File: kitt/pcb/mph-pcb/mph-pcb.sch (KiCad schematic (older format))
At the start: 121 parts, among them J1 Screw_Terminal_01x02, J2 Screw_Terminal_01x03, U1 TLC5940NT, U2 TLC5940NT, U3 TLC5940NT, U4 TLC5940NT, U5 TLC5940NT, U6 TLC5940NT, U7 TLC5940NT

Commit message: sed to get flangeless led
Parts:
- D25, D26, D27, HT1, HT10, HT11, HT12, HT13, HT14, HT15, HT16, HT2, HT3, HT4, HT5, HT6, HT7, HT8, HT9, HY1, HY2, HY3, MY1, MY2, MY3, UG1, UG10, UG11, UG12, UG13, UG14, UG15, UG16, UG17, UG18, UG19, UG2, UG20, UG3, UG4, UG5, UG6, UG7, UG8, UG9, UGY1, UGY2, UGY3: footprint (none) -> KITT-Footpads:Flangeless_LED

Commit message: added screw terminals
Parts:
- GUID1, GUID2, SYST1, SYST2: footprint (none) -> KITT-Footpads:DF3GD_Light_Bar
- J1: footprint (none) -> KITT-Footpads:5mm_Screw_Terminal_01x02
- J2: footprint (none) -> KITT-Footpads:5mm_Screw_Terminal_01x03
- MPH1, MPH2, MPH3: footprint (none) -> KITT-Footpads:KB2855SGD_Light_Square
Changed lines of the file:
@@
 F 0 "SYST2" H 9628 5046 50  0000 L CNN
 F 1 "DF3GD" H 9628 4955 50  0000 L CNN
-F 2 "" H 9500 5350 50  0001 C CNN
+F 2 "KITT-Footpads:DF3GD_Light_Bar" H 9500 5350 50  0001 C CNN
 F 3 "" H 9500 5350 50  0001 C CNN
 	1    9300 5000
@@
 F 0 "SYST1" H 8578 5046 50  0000 L CNN
 F 1 "DF3GD" H 8578 4955 50  0000 L CNN
-F 2 "" H 8450 5350 50  0001 C CNN
+F 2 "KITT-Footpads:DF3GD_Light_Bar" H 8450 5350 50  0001 C CNN
 F 3 "" H 8450 5350 50  0001 C CNN
 	1    8250 5000
@@
 F 0 "GUID2" H 9628 3696 50  0000 L CNN
 F 1 "DF3GD" H 9628 3605 50  0000 L CNN
-F 2 "" H 9500 4000 50  0001 C CNN
+F 2 "KITT-Footpads:DF3GD_Light_Bar" H 9500 4000 50  0001 C CNN
 F 3 "" H 9500 4000 50  0001 C CNN
 	1    9300 3650
@@
 F 0 "GUID1" H 8578 3696 50  0000 L CNN
 F 1 "DF3GD" H 8578 3605 50  0000 L CNN
-F 2 "" H 8450 4000 50  0001 C CNN
+F 2 "KITT-Footpads:DF3GD_Light_Bar" H 8450 4000 50  0001 C CNN
 F 3 "" H 8450 4000 50  0001 C CNN
 	1    8250 3650
@@
 F 0 "J1" H 1618 13467 50  0000 C CNN
 F 1 "Screw_Terminal_01x02" H 1618 13376 50  0000 C CNN
-F 2 "" H 1700 13250 50  0001 C CNN
+F 2 "KITT-Footpads:5mm_Screw_Terminal_01x02" H 1700 13250 50  0001 C CNN
 F 3 "~" H 1700 13250 50  0001 C CNN
 	1    1700 13250
@@
 F 0 "MPH1" H 18228 4546 50  0000 L CNN
 F 1 "KB2855SGD" H 18228 4455 50  0000 L CNN
-F 2 "" H 17400 4600 50  0001 C CNN
+F 2 "KITT-Footpads:KB2855SGD_Light_Square" H 17400 4600 50  0001 C CNN
 F 3 "" H 17400 4600 50  0001 C CNN
 	1    17800 4500
@@
 F 0 "MPH2" H 19528 4546 50  0000 L CNN
 F 1 "KB2855SGD" H 19528 4455 50  0000 L CNN
-F 2 "" H 18700 4600 50  0001 C CNN
+F 2 "KITT-Footpads:KB2855SGD_Light_Square" H 18700 4600 50  0001 C CNN
 F 3 "" H 18700 4600 50  0001 C CNN
 	1    19100 4500
@@
 F 0 "MPH3" H 20828 4546 50  0000 L CNN
 F 1 "KB2855SGD" H 20828 4455 50  0000 L CNN
-F 2 "" H 20000 4600 50  0001 C CNN
+F 2 "KITT-Footpads:KB2855SGD_Light_Square" H 20000 4600 50  0001 C CNN
 F 3 "" H 20000 4600 50  0001 C CNN
 	1    20400 4500
@@
 F 0 "J2" H 1668 14817 50  0000 C CNN
 F 1 "Screw_Terminal_01x03" H 1668 14726 50  0000 C CNN
-F 2 "" H 1750 14500 50  0001 C CNN
+F 2 "KITT-Footpads:5mm_Screw_Terminal_01x03" H 1750 14500 50  0001 C CNN
 F 3 "~" H 1750 14500 50  0001 C CNN
 	1    1750 14500

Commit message: add footpad for logic level shifter
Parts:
- LVL1: footprint (none) -> KITT-Footpads:LVL_5V_3V3
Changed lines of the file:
@@
 F 0 "LVL1" H 3250 15025 50  0000 C CNN
 F 1 "LVL_5V_3V3" H 3250 14934 50  0000 C CNN
-F 2 "" H 3250 14500 50  0001 C CNN
+F 2 "KITT-Footpads:LVL_5V_3V3" H 3250 14500 50  0001 C CNN
 F 3 "" H 3250 14500 50  0001 C CNN
 	1    3250 14500

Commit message: initial placement
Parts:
- renumbered D25 to MSGY1, D26 to MSGY2, D27 to MSGY3
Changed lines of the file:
@@
 	11750 1850 11750 1450
 $Comp
-L Device:LED D25
+L Device:LED MSGY1
 U 1 1 619E187B
 P 11750 6050
-F 0 "D25" V 11789 5932 50  0000 R CNN
+F 0 "MSGY1" V 11789 5932 50  0000 R CNN
 F 1 "LED" V 11698 5932 50  0000 R CNN
 F 2 "KITT-Footpads:Flangeless_LED" H 11750 6050 50  0001 C CNN
@@
 $EndComp
 $Comp
-L Device:LED D26
+L Device:LED MSGY2
 U 1 1 619E1881
 P 12100 6050
-F 0 "D26" V 12139 5932 50  0000 R CNN
+F 0 "MSGY2" V 12139 5932 50  0000 R CNN
 F 1 "LED" V 12048 5932 50  0000 R CNN
 F 2 "KITT-Footpads:Flangeless_LED" H 12100 6050 50  0001 C CNN
@@
 $EndComp
 $Comp
-L Device:LED D27
+L Device:LED MSGY3
 U 1 1 619E1887
 P 12450 6050
-F 0 "D27" V 12489 5932 50  0000 R CNN
+F 0 "MSGY3" V 12489 5932 50  0000 R CNN
 F 1 "LED" V 12398 5932 50  0000 R CNN
 F 2 "KITT-Footpads:Flangeless_LED" H 12450 6050 50  0001 C CNN

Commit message: add net ties for coupling caps
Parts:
- added NT1, NT2, NT3, NT4, NT5, NT6, NT7: Net-Tie_3_Tee, NetTie:NetTie-3_THT_Pad0.3mm, symbol Device:Net-Tie_3_Tee
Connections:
- net +5V: now also NT1.1, NT2.1, NT3.1, NT4.1, NT5.1, NT6.1, NT7.1; no longer C3.1, C4.1, C5.1, C6.1, C7.1, C8.1, C9.1, U1.21 (VCC), U2.21 (VCC), U3.21 (VCC), U4.21 (VCC), U5.21 (VCC), U6.21 (VCC), U7.21 (VCC)
- new net: NT1.2, U1.21 (VCC)
- new net: C3.1, NT1.3
- new net: NT2.2, U2.21 (VCC)
- new net: NT3.2, U3.21 (VCC)
- new net: C4.1, NT2.3
- new net: C5.1, NT3.3
- new net: C6.1, NT4.3
- new net: NT4.2, U4.21 (VCC)
- new net: NT5.2, U5.21 (VCC)
- new net: NT6.2, U6.21 (VCC)
- new net: C7.1, NT5.3
- new net: NT7.2, U7.21 (VCC)
- new net: C8.1, NT6.3
- new net: C9.1, NT7.3
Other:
- moved on the sheet: C3, C4, C5, C6, C7, C8, C9

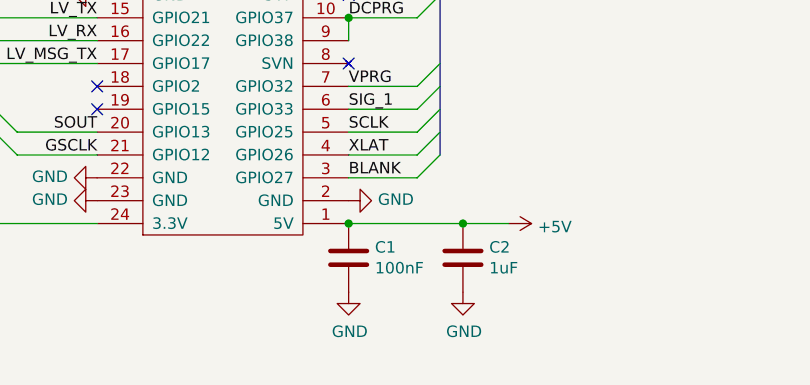
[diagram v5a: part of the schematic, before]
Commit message: routed led display chips
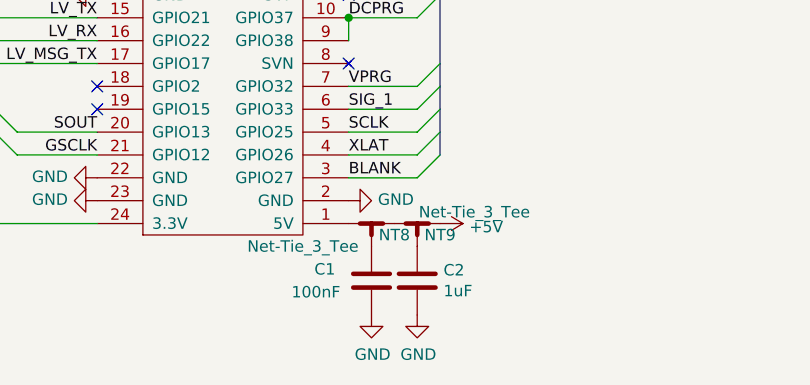
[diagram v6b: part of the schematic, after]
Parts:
- added NT8, NT9: Net-Tie_3_Tee, symbol Device:Net-Tie_3_Tee
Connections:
- net +5V: now also NT9.2; no longer C1.1, C2.1, TTGO1.1 (5V)
- new net: NT8.1, TTGO1.1 (5V)
- new net: C2.1, NT9.3
- new net: C1.1, NT8.3
- new net: NT8.2, NT9.1
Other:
- moved on the sheet: C1, C2
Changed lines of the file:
@@
 L power:+5V #PWR0108
 U 1 1 61112410
-P 6450 15300
-F 0 "#PWR0108" H 6450 15150 50  0001 C CNN
-F 1 "+5V" V 6465 15428 50  0000 L CNN
-F 2 "" H 6450 15300 50  0001 C CNN
-F 3 "" H 6450 15300 50  0001 C CNN
-	1    6450 15300
+P 6150 15300
+F 0 "#PWR0108" H 6150 15150 50  0001 C CNN
+F 1 "+5V" V 6165 15428 50  0000 L CNN
+F 2 "" H 6150 15300 50  0001 C CNN
+F 3 "" H 6150 15300 50  0001 C CNN
+	1    6150 15300
 	0    1    1    0
 $EndComp
@@
 	1    0    0    -1
 $EndComp
-Wire Wire Line
-	5750 15300 6250 15300
 $Comp
 L Device:C C1
 U 1 1 611E1B9E
-P 5750 15450
-F 0 "C1" H 5865 15496 50  0000 L CNN
-F 1 "100nF" H 5865 15405 50  0000 L CNN
-F 2 "Capacitor_THT:C_Rect_L7.0mm_W3.5mm_P5.00mm" H 5788 15300 50  0001 C CNN
-F 3 "~" H 5750 15450 50  0001 C CNN
-	1    5750 15450
+P 5850 15550
+F 0 "C1" H 5600 15600 50  0000 L CNN
+F 1 "100nF" H 5500 15500 50  0000 L CNN
+F 2 "Capacitor_THT:C_Rect_L7.0mm_W3.5mm_P5.00mm" H 5888 15400 50  0001 C CNN
+F 3 "~" H 5850 15550 50  0001 C CNN
+	1    5850 15550
 	1    0    0    -1
 $EndComp
-Connection ~ 5750 15300
 $Comp
 L power:GND #PWR0139
 U 1 1 611E2E2D
-P 5750 15600
-F 0 "#PWR0139" H 5750 15350 50  0001 C CNN
-F 1 "GND" H 5755 15427 50  0000 C CNN
-F 2 "" H 5750 15600 50  0001 C CNN
-F 3 "" H 5750 15600 50  0001 C CNN
-	1    5750 15600
+P 5850 15700
+F 0 "#PWR0139" H 5850 15450 50  0001 C CNN
+F 1 "GND" H 5855 15527 50  0000 C CNN
+F 2 "" H 5850 15700 50  0001 C CNN
+F 3 "" H 5850 15700 50  0001 C CNN
+	1    5850 15700
 	1    0    0    -1
 $EndComp
@@
 L Device:C C2
 U 1 1 61117E3E
-P 6250 15450
-F 0 "C2" H 6365 15496 50  0000 L CNN
-F 1 "1uF" H 6365 15405 50  0000 L CNN
-F 2 "Capacitor_THT:C_Rect_L7.0mm_W3.5mm_P5.00mm" H 6288 15300 50  0001 C CNN
-F 3 "~" H 6250 15450 50  0001 C CNN
-	1    6250 15450
+P 6050 15550
+F 0 "C2" H 6165 15596 50  0000 L CNN
+F 1 "1uF" H 6165 15505 50  0000 L CNN
+F 2 "Capacitor_THT:C_Rect_L7.0mm_W3.5mm_P5.00mm" H 6088 15400 50  0001 C CNN
+F 3 "~" H 6050 15550 50  0001 C CNN
+	1    6050 15550
 	1    0    0    -1
 $EndComp
-Connection ~ 6250 15300
 $Comp
 L power:GND #PWR0140
 U 1 1 611191EF
-P 6250 15600
-F 0 "#PWR0140" H 6250 15350 50  0001 C CNN
-F 1 "GND" H 6255 15427 50  0000 C CNN
-F 2 "" H 6250 15600 50  0001 C CNN
-F 3 "" H 6250 15600 50  0001 C CNN
-	1    6250 15600
+P 6050 15700
+F 0 "#PWR0140" H 6050 15450 50  0001 C CNN
+F 1 "GND" H 6055 15527 50  0000 C CNN
+F 2 "" H 6050 15700 50  0001 C CNN
+F 3 "" H 6050 15700 50  0001 C CNN
+	1    6050 15700
 	1    0    0    -1
 $EndComp
-Wire Wire Line
-	6450 15300 6250 15300
 $Comp
 L Device:LED HT1
@@
 	0    -1   -1   0
 $EndComp
+$Comp
+L Device:Net-Tie_3_Tee NT8
+U 1 1 6145D0D2
+P 5850 15300
+F 0 "NT8" H 5950 15250 50  0000 C CNN
+F 1 "Net-Tie_3_Tee" H 5550 15200 50  0000 C CNN
+F 2 "" H 5850 15300 50  0001 C CNN
+F 3 "~" H 5850 15300 50  0001 C CNN
+	1    5850 15300
+	1    0    0    -1
+$EndComp
+$Comp
+L Device:Net-Tie_3_Tee NT9
+U 1 1 614619B6
+P 6050 15300
+F 0 "NT9" H 6150 15250 50  0000 C CNN
+F 1 "Net-Tie_3_Tee" H 6300 15350 50  0000 C CNN
+F 2 "" H 6050 15300 50  0001 C CNN
+F 3 "~" H 6050 15300 50  0001 C CNN
+	1    6050 15300
+	1    0    0    -1
+$EndComp
 Wire Bus Line

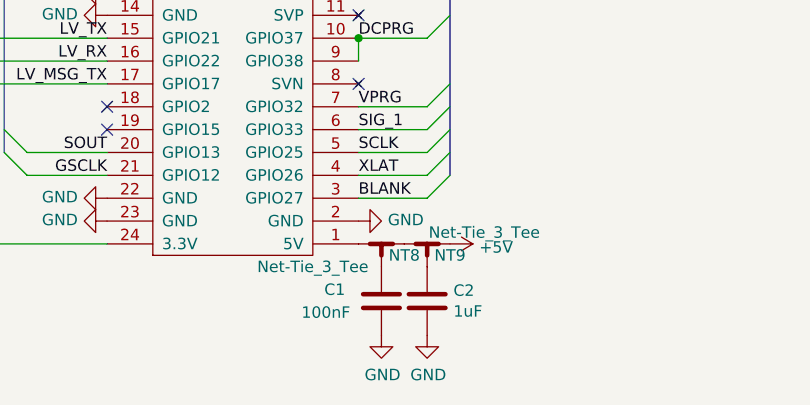
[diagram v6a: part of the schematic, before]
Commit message: finshed mph placement
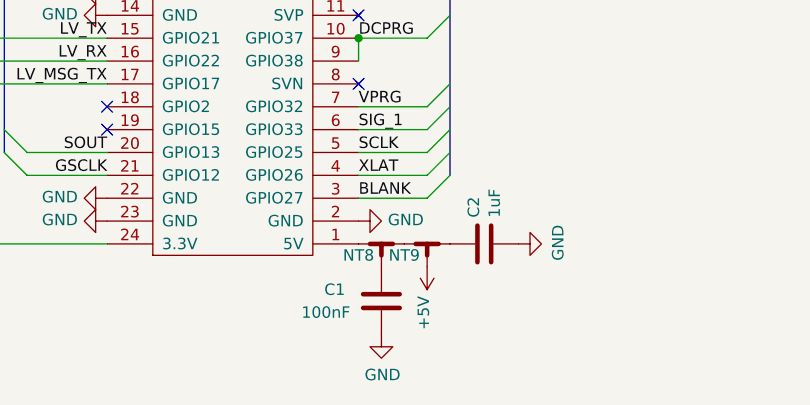
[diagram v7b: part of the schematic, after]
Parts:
- NT8, NT9: footprint (none) -> NetTie:NetTie-3_THT_Pad0.3mm
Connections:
- net +5V: now also NT9.3; no longer NT9.2
- net at C2.1: now also NT9.1; no longer NT9.3
- net at NT8.2: now also NT9.2; no longer NT9.1
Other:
- moved on the sheet: C2
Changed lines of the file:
@@
 L power:+5V #PWR0108
 U 1 1 61112410
-P 6150 15300
-F 0 "#PWR0108" H 6150 15150 50  0001 C CNN
-F 1 "+5V" V 6165 15428 50  0000 L CNN
-F 2 "" H 6150 15300 50  0001 C CNN
-F 3 "" H 6150 15300 50  0001 C CNN
-	1    6150 15300
-	0    1    1    0
+P 6050 15400
+F 0 "#PWR0108" H 6050 15250 50  0001 C CNN
+F 1 "+5V" V 6065 15528 50  0000 L CNN
+F 2 "" H 6050 15400 50  0001 C CNN
+F 3 "" H 6050 15400 50  0001 C CNN
+	1    6050 15400
+	-1   0    0    1
 $EndComp
 $Comp
@@
 L Device:C C2
 U 1 1 61117E3E
-P 6050 15550
-F 0 "C2" H 6165 15596 50  0000 L CNN
-F 1 "1uF" H 6165 15505 50  0000 L CNN
-F 2 "Capacitor_THT:C_Rect_L7.0mm_W3.5mm_P5.00mm" H 6088 15400 50  0001 C CNN
-F 3 "~" H 6050 15550 50  0001 C CNN
-	1    6050 15550
-	1    0    0    -1
+P 6300 15300
+F 0 "C2" H 6415 15346 50  0000 L CNN
+F 1 "1uF" H 6415 15255 50  0000 L CNN
+F 2 "Capacitor_THT:C_Rect_L7.0mm_W3.5mm_P5.00mm" H 6338 15150 50  0001 C CNN
+F 3 "~" H 6300 15300 50  0001 C CNN
+	1    6300 15300
+	0    -1   -1   0
 $EndComp
 $Comp
 L power:GND #PWR0140
 U 1 1 611191EF
-P 6050 15700
-F 0 "#PWR0140" H 6050 15450 50  0001 C CNN
-F 1 "GND" H 6055 15527 50  0000 C CNN
-F 2 "" H 6050 15700 50  0001 C CNN
-F 3 "" H 6050 15700 50  0001 C CNN
-	1    6050 15700
-	1    0    0    -1
+P 6450 15300
+F 0 "#PWR0140" H 6450 15050 50  0001 C CNN
+F 1 "GND" H 6455 15127 50  0000 C CNN
+F 2 "" H 6450 15300 50  0001 C CNN
+F 3 "" H 6450 15300 50  0001 C CNN
+	1    6450 15300
+	0    -1   -1   0
 $EndComp
 $Comp
@@
 $EndComp
 $Comp
-L power:+5V #PWR?
+L power:+5V #PWR0110
 U 1 1 6128F951
 P 6600 11850
-F 0 "#PWR?" H 6600 11700 50  0001 C CNN
+F 0 "#PWR0110" H 6600 11700 50  0001 C CNN
 F 1 "+5V" H 6615 12023 50  0000 C CNN
 F 2 "" H 6600 11850 50  0001 C CNN
@@
 $EndComp
 $Comp
-L power:+5V #PWR?
+L power:+5V #PWR0113
 U 1 1 612F8EB9
 P 9200 11850
-F 0 "#PWR?" H 9200 11700 50  0001 C CNN
+F 0 "#PWR0113" H 9200 11700 50  0001 C CNN
 F 1 "+5V" H 9215 12023 50  0000 C CNN
 F 2 "" H 9200 11850 50  0001 C CNN
@@
 $EndComp
 $Comp
-L power:+5V #PWR?
+L power:+5V #PWR0116
 U 1 1 61392955
 P 11800 11850
-F 0 "#PWR?" H 11800 11700 50  0001 C CNN
+F 0 "#PWR0116" H 11800 11700 50  0001 C CNN
 F 1 "+5V" H 11815 12023 50  0000 C CNN
 F 2 "" H 11800 11850 50  0001 C CNN
@@
 $EndComp
 $Comp
-L power:+5V #PWR?
+L power:+5V #PWR0119
 U 1 1 613FBBB5
 P 14400 11850
-F 0 "#PWR?" H 14400 11700 50  0001 C CNN
+F 0 "#PWR0119" H 14400 11700 50  0001 C CNN
 F 1 "+5V" H 14415 12023 50  0000 C CNN
 F 2 "" H 14400 11850 50  0001 C CNN
@@
 $EndComp
 $Comp
-L power:+5V #PWR?
+L power:+5V #PWR0122
 U 1 1 61461A21
 P 17000 11850
-F 0 "#PWR?" H 17000 11700 50  0001 C CNN
+F 0 "#PWR0122" H 17000 11700 50  0001 C CNN
 F 1 "+5V" H 17015 12023 50  0000 C CNN
 F 2 "" H 17000 11850 50  0001 C CNN
@@
 $EndComp
 $Comp
-L power:+5V #PWR?
+L power:+5V #PWR0125
 U 1 1 614C69AB
 P 19600 11850
-F 0 "#PWR?" H 19600 11700 50  0001 C CNN
+F 0 "#PWR0125" H 19600 11700 50  0001 C CNN
 F 1 "+5V" H 19615 12023 50  0000 C CNN
 F 2 "" H 19600 11850 50  0001 C CNN
@@
 U 1 1 6145D0D2
 P 5850 15300
-F 0 "NT8" H 5950 15250 50  0000 C CNN
-F 1 "Net-Tie_3_Tee" H 5550 15200 50  0000 C CNN
-F 2 "" H 5850 15300 50  0001 C CNN
+F 0 "NT8" H 5750 15250 50  0000 C CNN
+F 1 "Net-Tie_3_Tee" H 5550 15200 50  0001 C CNN
+F 2 "NetTie:NetTie-3_THT_Pad0.3mm" H 5850 15300 50  0001 C CNN
 F 3 "~" H 5850 15300 50  0001 C CNN
 	1    5850 15300
@@
 P 6050 15300
 F 0 "NT9" H 6150 15250 50  0000 C CNN
-F 1 "Net-Tie_3_Tee" H 6300 15350 50  0000 C CNN
-F 2 "" H 6050 15300 50  0001 C CNN
+F 1 "Net-Tie_3_Tee" H 6300 15350 50  0001 C CNN
+F 2 "NetTie:NetTie-3_THT_Pad0.3mm" H 6050 15300 50  0001 C CNN
 F 3 "~" H 6050 15300 50  0001 C CNN
 	1    6050 15300
-	1    0    0    -1
+	-1   0    0    -1
 $EndComp
 Wire Bus Line

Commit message: more wiring
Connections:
- net BLANK: now also TTGO1.7 (GPIO32); no longer TTGO1.3 (GPIO27)
- net SCLK: now also TTGO1.4 (GPIO26); no longer TTGO1.5 (GPIO25)
- net VPRG: now also TTGO1.3 (GPIO27); no longer TTGO1.7 (GPIO32)
- net XLAT: now also TTGO1.5 (GPIO25); no longer TTGO1.4 (GPIO26)
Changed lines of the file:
@@
 $EndComp
 Text Label 5750 15100 0    50   ~ 0
-BLANK
+VPRG
 Text Label 5750 15000 0    50   ~ 0
+SCLK
+Text Label 5750 14900 0    50   ~ 0
 XLAT
-Text Label 5750 14900 0    50   ~ 0
-SCLK
 Text Label 5750 14800 0    50   ~ 0
 SIG_1
 Text Label 5750 14700 0    50   ~ 0
-VPRG
+BLANK
 Text Label 4650 15000 2    50   ~ 0
 GSCLK
